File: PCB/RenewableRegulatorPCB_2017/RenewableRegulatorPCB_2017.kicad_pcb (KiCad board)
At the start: 2 copper layers, 77.5 x 81.9 mm, 59 parts, among them IC2 ATTINY85, K1 IO_0-2, K2 IO_3-5, K3 Vsense, K4 Vpower, P1 FTDI_OUTPUT, P11 Voutput, P12 Vsense, P13 OUT, P14 FET_IN, P2 IN, P3 Vinput, P4 5V, P5 ISP, P6 GND, P7 S_INPUT, P8 Vd, P9 Vg, Q1 PNP, Q2 NPN, Q3 MOSFET_N, SW1 SW_PUSH, U1 7805/LM2931, U2 LM7812, U3 AUIRS2124

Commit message: Updated PCB
First version of schematic. Needs review
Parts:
- removed BZ1: BUZZER, BUZZER_lg_pads
- removed IC2: ATTINY85, TRINKET
- removed K1: IO_0-2, SIL-3_lg_pad_1mm
- removed K2: IO_3-5, SIL-3_lg_pad_1mm
- removed K3: Vsense, SIL-3_lg_pad_1mm_marker
- removed K4: Vpower, SIL-3_lg_pad_1mm_marker
- removed MH1, MH2, MH3, MH4: CONN_1, 1pin_3mmhole
- removed P11: Voutput, 1pin_1.2mm
- removed P12: Vsense, 1pin_1.2mm
- removed P13: OUT, SIL_2_screw_blocks
- removed P14: FET_IN, 1pin_1.2mm
- removed P6: GND, 1pin_1.2mm
- removed P7: S_INPUT, SIL-6_large_pads_marker
- removed P8: Vd, 1pin_1.2mm
- removed P9: Vg, 1pin_1.2mm
- removed Q2: NPN, TO92-EBC_large_pad
- removed Q3: MOSFET_N, TO220_VERT_BUZ11_matt
- removed SW1: SW_PUSH, SW_PUSH_SMALL_ml_large_hole
- removed VAL: OSHW_logo_small_back, OSHW_logo_small_back
- removed VAL: reinnovation_logo_15mm, reinnovation_logo_15mm
- added C10: 10uf, REInnovationFootprint:C_1V7_TH, F.Cu at (114.9, 95.9)
- added C9: 1uf, REInnovationFootprint:C_1V7_TH, F.Cu at (108.6, 85.7)
- added DISP1: OLED_I2C, matts_components:SIL-4_large_pad, F.Cu at (153.7, 130.8)
- added DISP2: SPI_LCD, matts_components:SIL-8_lg_pad_1mm, F.Cu at (195.6, 84.5)
- added ENC1: Encoder, REInnovationFootprint:TH_Encoder, F.Cu at (135.3, 153.7)
- added F1: 1A, REInnovationFootprint:TH_MC36188_FUSE, F.Cu at (145.4, 119.4)
- added J1: Arduino_Nano_Header, REInnovationFootprint:NANO_DIP_30_600, F.Cu at (227.3, 109.9)
- added L1: 22uH, REInnovationFootprint:TH_Inductor, F.Cu at (167.0, 136.5)
- added LOGO1: CONN_1, CuriousElectric3:CEC_Globe_10mm_FCU, F.Cu at (56.5, 163.8)
- added LOGO2: CONN_1, CuriousElectric3:CuriousElectric_flat_12mm, F.Cu at (55.2, 155.6)
- added R10: 8.2k, REInnovationFootprint:TH_Resistor_1, F.Cu at (174.0, 111.1)
- added VR2: VR, REInnovationFootprint:TH_MC36188_FUSE, F.Cu at (125.7, 98.4)
- C1: value 10uf -> 100nf; footprint C1V7_lg_pad -> matts_components:C1_wide_lg_pad
- C2: value 100u -> 100nf; footprint C1V7_lg_pad -> matts_components:C1_wide_lg_pad
- C3: value 100n -> 100uf; footprint C1_wide_lg_pad -> REInnovationFootprint:C_1V7_TH
- C4, C5: value 10u -> 100nf; footprint C1V7_lg_pad -> matts_components:C1_wide_lg_pad
- C6: value 10u -> 2.2uf; footprint C1V7_lg_pad -> REInnovationFootprint:C_1V7_TH
- C7: value 100n -> 1uf; footprint C1_wide_lg_pad -> REInnovationFootprint:C_1V7_TH
- C8: value CP1 -> 100nf; footprint C1V7_lg_pad -> matts_components:C1_wide_lg_pad
- D1, D2: value 1N4001 -> 3v3; footprint D4_lg_pad -> REInnovationFootprint:TH_Diode_1
- D3: value VT2045BP -> 1N5819; footprint TO220_DIODE -> REInnovationFootprint:TH_Diode_1
- D4: value 1N4001 -> 1N5819; footprint D4_lg_pad -> REInnovationFootprint:TH_Diode_1
- D5: value 1N4148 -> WS2811_5mm; footprint D3_lg_pad -> REInnovationFootprint:TH_WS2811_LED_8mm
- D6: value UF4001 -> 1N5822; footprint D4_lg_pad -> REInnovationFootprint:TH_Diode_1
- D7: value 5v1 -> LED; footprint D3_lg_pad -> REInnovationFootprint:TH_LED-5MM_larg_pad
- D8: value DIODE -> UF4001; footprint D3_lg_pad -> REInnovationFootprint:TH_Diode_1
- D9: value GRN_LED -> 1N5819; footprint LED-5MM_larg_pad -> REInnovationFootprint:TH_Diode_1
- P1: value FTDI_OUTPUT -> INPUT; footprint SIL-6_large_pads_marker -> matts_components:SIL-2_screw_terminal_32A
- P2: value IN -> Vref?; footprint SIL_2_screw_blocks -> matts_components:SIL-2_solder_connect
- P3: value Vinput -> MicroSD; footprint 1pin_1.2mm -> matts_components:SIL-6_large_pads_marker
- P4: value 5V -> SERIAL; footprint 1pin_1.2mm -> matts_components:SIL-4_Grove_SIL
- P5: value ISP -> OUTPUT; footprint DIL_3x2_large_pads_1mm -> matts_components:SIL-2_screw_terminal_32A
- Q1: value PNP -> TK32A12N1; footprint TO92-EBC_large_pad -> matts_components:TO220_VERT_BUZ11_matt
- R1, R4: value 1k -> R; footprint R3-LARGE_PADS_0_8_hole -> REInnovationFootprint:TH_Resistor_1
- R2: value 100k -> R; footprint R3-LARGE_PADS_0_8_hole -> REInnovationFootprint:TH_Resistor_1
- R3: value 10k -> R; footprint R3-LARGE_PADS_0_8_hole -> REInnovationFootprint:TH_Resistor_1
- R5: value 10k -> 5; footprint R3-LARGE_PADS_0_8_hole -> REInnovationFootprint:TH_Resistor_1
- R6: value 330 -> 1k; footprint R3-LARGE_PADS_0_8_hole -> REInnovationFootprint:TH_Resistor_1
- R7, R8: value R -> 100k; footprint R3-LARGE_PADS_0_8_hole -> REInnovationFootprint:TH_Resistor_1
- R9: value 10 -> 100k; footprint R3-LARGE_PADS_0_8_hole -> REInnovationFootprint:TH_Resistor_1
- U1: value 7805/LM2931 -> IR2117; footprint TO92_7805_matt -> REInnovationFootprint:DIP-8_300_ELL
- U2: value LM7812 -> LMR16006; footprint TO92_7805_matt -> matts_components:SOT23-5_matt
- U3: value AUIRS2124 -> MCP1702-50; footprint SO8E -> matts_components:TO92_MCP9701_matt
- VR1: value P6KE33CA-E3 -> VR; footprint D4_lg_pad -> REInnovationFootprint:TH_MC36188_FUSE
- moved U1 102.7 mm to (203.2, 134.0), turned to 0 degrees
- moved C2 87.9 mm to (181.6, 143.5), turned to 0 degrees
- moved C3 83.8 mm to (84.5, 101.6), turned to 0 degrees
- moved C6 82.5 mm to (103.5, 133.3), turned to 0 degrees
- moved D3 78.9 mm to (144.1, 144.1), turned to 0 degrees
- moved P3 75.1 mm to (198.1, 89.5), turned to 0 degrees
- moved C8 66.7 mm to (94.0, 88.3), turned to 0 degrees
- moved D5 64.2 mm to (101.0, 71.8)
- moved R7 64.0 mm to (174.0, 103.5), turned to 0 degrees
- moved R8 59.9 mm to (174.0, 106.0), turned to 0 degrees
- moved Q1 59.0 mm to (182.9, 134.6), turned to 0 degrees
- moved C5 58.5 mm to (94.6, 83.8), turned to 0 degrees
- moved P4 58.1 mm to (127.0, 134.6)
- moved R6 58.0 mm to (174.0, 101.0), turned to 0 degrees
- moved D4 56.8 mm to (125.7, 71.8), turned to 0 degrees
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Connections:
- C1 pad 1: N-0000019 -> VINm
- C2 pad 1: +5V -> VOUTm
- C3 pad 1: GND -> Voutput
- C3 pad 2: +5V -> GND
- C4 pad 1: N-0000028 -> /Power Supply/+10V
- C5 pad 1: N-0000035 -> Net-(C5-Pad1)
- C5 pad 2: GND -> Voutput
- C6 pad 1: N-0000020 -> /Power Supply/+PWR
- C6 pad 2: Voutput -> GND
- C7 pad 1: SCK -> /Power Supply/+10V
- C8 pad 1: N-0000010 -> Net-(C8-Pad1)
- C8 pad 2: Voutput -> Net-(C8-Pad2)
- D1 pad 1: N-000009 -> GND
- D1 pad 2: N-0000019 -> VINm
- D2 pad 1: N-0000034 -> GND
- D2 pad 2: +5V -> VOUTm
- D3 pad 1: N-0000028 -> Net-(D3-Pad1)
- D3 pad 2: Vinput -> Voutput
- D4 pad 1: N-000008 -> Net-(D3-Pad1)
- D4 pad 2: +5V -> Vinput
- D5 pad 1: N-0000035 -> (no net)
- D5 pad 2: N-0000020 -> GND
- D6 pad 1: GND -> Net-(C5-Pad1)
- D6 pad 2: Voutput -> /Power Supply/+10V
- D7 pad 1: GND -> Voutput
- D7 pad 2: SCK -> Net-(D7-Pad2)
- D8 pad 1: N-0000035 -> GND
- D8 pad 2: N-0000010 -> Voutput
- D9 pad 1: N-000001 -> Net-(C8-Pad2)
- P1 pad 1: GND -> Vinput
- P2 pad 1: Vinput -> Net-(J1-Pad18)
- P2 pad 2: GND -> +3V3
- P3 pad 1: Vinput -> +3V3
- P4 pad 1: +5V -> GND
- P5 pad 1: LED -> Voutput
- P5 pad 2: N-000008 -> GND
- R1 pad 1: FET -> Vinput
- R1 pad 2: N-000007 -> VINm
- R2 pad 1: N-0000031 -> VINm
- R3 pad 1: N-0000031 -> Voutput
- R3 pad 2: N-000003 -> VOUTm
- R4 pad 1: N-0000020 -> VOUTm
- R4 pad 2: N-0000021 -> GND
- R5 pad 1: FET -> Net-(Q1-PadG)
- R5 pad 2: GND -> Net-(R5-Pad2)
- R6 pad 1: LED -> Net-(D7-Pad2)
- R6 pad 2: N-000001 -> GND
- R7 pad 1: N-000002 -> Net-(Q1-PadG)
- R7 pad 2: SCK -> Voutput
- R8 pad 1: SCK -> /Power Supply/+PWR
- R8 pad 2: GND -> Net-(R8-Pad2)
- R9 pad 1: N-0000011 -> /Power Supply/+10V
- R9 pad 2: N-0000021 -> Net-(R10-Pad1)
- VR1 pad 1: GND -> Vinput
- VR1 pad 2: N-0000028 -> GND
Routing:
- net GND: track 270.7 -> 0.00 mm, vias 1 -> 0
- net Voutput: track 225.9 -> 0.00 mm, vias 2 -> 0
- net Vinput: track 174.6 -> 0.00 mm
- net +5V: track 136.9 -> 0.00 mm, vias 3 -> 0
- net Tx: track 125.5 -> 0.00 mm, vias 3 -> 0
- net Rx: track 121.1 -> 0.00 mm, vias 1 -> 0
- net SCK: track 98.5 -> 0.00 mm
- net LED: track 91.0 -> 0.00 mm, vias 2 -> 0
- net N-0000028: track 62.4 -> 0.00 mm
- net FET: track 62.3 -> 0.00 mm
- net N-0000021: track 52.0 -> 0.00 mm
- net RESET: track 46.8 -> 0.00 mm
- net N-0000035: track 42.8 -> 0.00 mm, vias 1 -> 0
- net N-0000031: track 22.4 -> 0.00 mm
- net N-0000010: track 19.4 -> 0.00 mm
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- removed copper zone on B.Cu, net GND
- removed copper zone on F.Cu, net GND
- removed copper zone on F.Cu, net N-0000028
- removed copper zone on B.Cu, net Vinput
- removed copper zone on B.Cu, net Voutput
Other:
- board outline removed
- board text removed: "5/12/13 V1.2"
- board text removed: "DIODE"
- board text removed: "FET"
- board text removed: "I/O"
- board text removed: "Open Charge Regulator"
- board text removed: "TRINKET"
- board text removed: "re-innovation.co.uk"
- board text removed: "samaenergy.org"
- board text removed: "uP"

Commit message: Large update of PCB design
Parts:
- added J2: Arduino_Nano_Header, REInnovationFootprint:NANO_DIP_30_600, F.Cu at (153.7, 102.9)
- added P10: TP_FET, matts_components:1pin_0_8mm, F.Cu at (88.3, 121.3)
- added P11: TP_GND, matts_components:1pin_0_8mm, F.Cu at (78.7, 81.3)
- added P12: TP_5V, matts_components:1pin_0_8mm, F.Cu at (108.6, 59.1)
- added P13: TP_10V, matts_components:1pin_0_8mm, F.Cu at (104.1, 74.3)
- added P6: SERIAL, matts_components:SIL-4_Grove_SIL, F.Cu at (166.4, 87.6)
- added P7: A2, matts_components:SIL-4_Grove_SIL, F.Cu at (166.4, 78.1)
- added P8: TP_Vin, matts_components:1pin_0_8mm, F.Cu at (123.8, 84.5)
- added P9: TP_Vout, matts_components:1pin_0_8mm, F.Cu at (118.7, 108.6)
- added PCB1: PCB, REInnovationFootprint:PCB_75x100mm, F.Cu at (175.9, 130.2)
- added R11: 8.2k, REInnovationFootprint:TH_Resistor_1, F.Cu at (99.7, 81.3)
- DISP1: footprint matts_components:SIL-4_large_pad -> REInnovationFootprint:TH_OLED1306
- DISP2: footprint matts_components:SIL-8_lg_pad_1mm -> REInnovationFootprint:TH_LCD_SPI_128x128
- J1: value Arduino_Nano_Header -> JACK_TRS_6PINS; footprint REInnovationFootprint:NANO_DIP_30_600 -> REInnovationFootprint:TH_3_5mm_Jack
- LOGO1: value CONN_1 -> LOGO
- LOGO2: value CONN_1 -> LOGO; footprint CuriousElectric3:CuriousElectric_flat_12mm -> CuriousElectric3:TCEC_Words_13mm
- P4: value SERIAL -> A6_7
- R1, R3: value R -> Rb
- R10: value 8.2k -> 100k
- R2, R4: value R -> Ra
- R5: value 5 -> 4k7
- R6: value 1k -> 5
- R7: value 100k -> 1k
- U2: footprint matts_components:SOT23-5_matt -> REInnovationFootprint:SM_SOT23-6
- moved LOGO1 129.4 mm to (151.1, 75.6)
- moved U1 121.2 mm to (86.4, 101.6), turned to 180 degrees
- moved LOGO2 116.8 mm to (145.4, 81.3)
- moved U3 112.9 mm to (95.9, 59.7), turned to 180 degrees
- moved Q1 107.8 mm to (78.7, 106.7), turned to 180 degrees
- moved L1 95.2 mm to (98.4, 70.5)
- moved P1 92.3 mm to (88.9, 137.2)
- moved R7 90.4 mm to (85.7, 123.2), turned to 270 degrees
- moved R9 90.0 mm to (88.3, 81.3), turned to 270 degrees
- moved R8 86.1 mm to (88.3, 113.7), turned to 90 degrees
- moved R6 83.5 mm to (91.4, 113.7), turned to 90 degrees
- moved R10 83.0 mm to (96.5, 81.3), turned to 270 degrees
- moved U2 82.7 mm to (82.5, 78.1), turned to 270 degrees
- moved P4 76.9 mm to (166.4, 68.6)
- moved C2 74.5 mm to (118.7, 103.5), turned to 90 degrees
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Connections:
- J1 pad 1: Tx -> GND
- J1 pad 2: Rx -> +5V
- J1 pad 3: (no net) -> TEMP
- J1 pad 5: EN_A -> (no net)
- J1 pad 6: EN_B -> (no net)
- P2 pad 1: Net-(J1-Pad18) -> Net-(J2-Pad18)
- P4 pad 3: Tx -> A7
- P4 pad 4: Rx -> A6
- Q1 pad G: Net-(Q1-PadG) -> Net-(P10-Pad1)
- R10 pad 1: Net-(R10-Pad1) -> /Power Supply/+10V
- R10 pad 2: GND -> Net-(R10-Pad2)
- R5 pad 1: Net-(Q1-PadG) -> +5V
- R5 pad 2: Net-(R5-Pad2) -> TEMP
- R6 pad 1: Net-(D7-Pad2) -> Net-(P10-Pad1)
- R6 pad 2: GND -> Net-(R6-Pad2)
- R7 pad 1: Net-(Q1-PadG) -> Net-(D7-Pad2)
- R7 pad 2: Voutput -> GND
- R8 pad 1: /Power Supply/+PWR -> Net-(P10-Pad1)
- R8 pad 2: Net-(R8-Pad2) -> Voutput
- R9 pad 1: /Power Supply/+10V -> /Power Supply/+PWR
- R9 pad 2: Net-(R10-Pad1) -> Net-(R9-Pad2)
- U1 pad 7: Net-(R5-Pad2) -> Net-(R6-Pad2)
- U2 pad 3: Net-(R10-Pad1) -> Net-(R10-Pad2)
- U2 pad 4: Net-(R8-Pad2) -> Net-(R9-Pad2)

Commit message: First Version of PCB
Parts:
- removed PCB1: PCB, REInnovationFootprint:PCB_75x100mm
- moved P7 102.0 mm to (70.5, 43.2), turned to 180 degrees
- moved P6 93.8 mm to (83.8, 43.2), turned to 180 degrees
- moved P3 80.1 mm to (147.3, 47.6), turned to 180 degrees
- moved P2 74.1 mm to (109.9, 46.4), turned to 90 degrees
- moved P4 73.7 mm to (97.2, 43.2), turned to 180 degrees
- moved R7 64.3 mm to (104.1, 61.6), turned to 90 degrees
- moved D8 59.2 mm to (108.0, 62.9), turned to 90 degrees
- moved J2 59.0 mm to (120.7, 54.0), turned to 90 degrees
- moved R6 55.9 mm to (89.5, 57.8), turned to 180 degrees
- moved D6 55.7 mm to (74.9, 50.8), turned to 0 degrees
- moved C5 55.3 mm to (96.5, 56.5)
- moved R8 53.4 mm to (100.3, 61.6), turned to 270 degrees
- moved D7 53.1 mm to (104.1, 70.5), turned to 270 degrees
- moved C4 44.7 mm to (67.3, 56.5), turned to 270 degrees
- moved LOGO2 43.6 mm to (157.5, 39.4)
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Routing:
- net GND: track 0.00 -> 575.2 mm
- net +5V: track 0.00 -> 244.0 mm, vias 0 -> 1
- net Voutput: track 0.00 -> 146.5 mm
- net TEMP: track 0.00 -> 145.8 mm, vias 0 -> 1
- net FET1: track 0.00 -> 107.0 mm
- net VOUTm: track 0.00 -> 105.0 mm
- net SCK: track 0.00 -> 100.5 mm, vias 0 -> 1
- net Rx: track 0.00 -> 94.9 mm, vias 0 -> 1
- net /Power Supply/+10V: track 0.00 -> 93.3 mm
- net Tx: track 0.00 -> 91.3 mm, vias 0 -> 1
- net Vinput: track 0.00 -> 86.8 mm
- net VINm: track 0.00 -> 86.6 mm
- net Net-(P10-Pad1): track 0.00 -> 80.7 mm
- net A7: track 0.00 -> 76.3 mm
- net A6: track 0.00 -> 74.3 mm
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- added copper zone on F.Cu, net Vinput
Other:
- net class Default: trace_width 2.54 -> 0.5

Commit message: Secod
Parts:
- C10: footprint REInnovationFootprint:C_1V7_TH -> RenewableRegulatorPCB_2017_Library_Yoan:Capacitor_C10_1V7_TH
- C3: footprint REInnovationFootprint:C_1V7_TH -> RenewableRegulatorPCB_2017_Library_Yoan:Capacitor_C_1V7_TH
- C6: footprint REInnovationFootprint:C_1V7_TH -> RenewableRegulatorPCB_2017_Library_Yoan:Capacitor_C6_1V7_TH
- C7: footprint REInnovationFootprint:C_1V7_TH -> RenewableRegulatorPCB_2017_Library_Yoan:Capacitor_C7_1V7_TH
- C9: footprint REInnovationFootprint:C_1V7_TH -> RenewableRegulatorPCB_2017_Library_Yoan:Capacitor_C9_1V7_TH
- P1, P5: footprint matts_components:SIL-2_screw_terminal_32A -> RenewableRegulatorPCB_2017_Library_Yoan:Connecteurs_IO_SIL-2_screw_terminal_32A
- moved LOGO2 103.8 mm to (71.6, 97.8)
- moved LOGO1 62.9 mm to (116.8, 75.4)
- moved D8 33.0 mm to (101.6, 95.2), turned to 180 degrees
- moved R7 30.1 mm to (100.3, 91.4), turned to 180 degrees
- moved R6 29.2 mm to (88.9, 87.0), turned to 90 degrees
- moved C9 26.9 mm to (103.8, 63.6), turned to 90 degrees
- moved R8 26.7 mm to (100.3, 88.3), turned to 0 degrees
- moved C5 26.4 mm to (92.1, 82.5)
- moved U1 26.3 mm to (75.6, 88.9)
- moved C4 26.0 mm to (66.7, 82.5)
- moved D6 26.0 mm to (74.9, 76.8)
- moved D7 23.9 mm to (111.1, 93.3)
- moved P1 17.6 mm to (90.2, 134.0)
- moved P5 17.6 mm to (111.8, 134.0)
- moved U3 15.2 mm to (103.8, 71.4), turned to 0 degrees
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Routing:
- net GND: track 575.2 -> 379.8 mm
- net TEMP: track 145.8 -> 80.6 mm, vias 1 -> 0
- net LED_D: track 33.8 -> 97.1 mm
- net SCK: track 100.5 -> 53.2 mm
- net VOUTm: track 105.0 -> 58.4 mm
- net +5V: track 244.0 -> 204.5 mm
- net A6: track 74.3 -> 35.8 mm, vias 0 -> 3
- net A7: track 76.3 -> 38.5 mm, vias 0 -> 4
- net Net-(P10-Pad1): track 80.7 -> 44.5 mm
- net SCL: track 61.6 -> 95.8 mm, vias 1 -> 2
- net Voutput: track 146.5 -> 123.8 mm
- net VINm: track 86.6 -> 68.2 mm
- net Rx: track 94.9 -> 80.5 mm, vias 1 -> 0
- net SD_CS: track 35.7 -> 21.8 mm, vias 0 -> 1
- net Vinput: track 86.8 -> 100.0 mm
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- added copper zone on B.Cu, net GND
- added copper zone on F.Cu, net GND
- added copper zone on F.Cu, net Voutput
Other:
- board outline added: 99.7 x 88.3 mm
- net class Thick: trace_width 5.08 -> 5

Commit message: Third Version of PCB
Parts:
- added MH1: CONN_1, RenewableRegulatorPCB_2017_Library_Yoan:3mm_hole, F.Cu at (161.0, 114.1)
- added MH1: CONN_1, RenewableRegulatorPCB_2017_Library_Yoan:3mm_hole, F.Cu at (161.0, 49.1)
- added MH1: CONN_1, RenewableRegulatorPCB_2017_Library_Yoan:3mm_hole, F.Cu at (66.0, 49.1)
- added MH1: CONN_1, RenewableRegulatorPCB_2017_Library_Yoan:3mm_hole, F.Cu at (66.0, 114.1)
- moved P7 4.79 mm to (72.9, 56.5)
- moved P6 2.10 mm to (85.3, 54.0)
- moved LOGO2 1.44 mm to (70.6, 96.8)
- moved P12 0.74 mm to (116.5, 92.1)
- moved DISP1 0.63 mm to (144.8, 64.8)
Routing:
- net GND: track 379.8 -> 363.9 mm
- net FET1: track 118.6 -> 114.7 mm
- net A2: track 49.9 -> 46.4 mm
- net +5V: track 204.5 -> 207.8 mm
- net Voutput: track 123.8 -> 126.3 mm
- net Rx: track 80.5 -> 81.3 mm
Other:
- board size 99.7 x 88.3 mm -> 101.3 x 88.3 mm

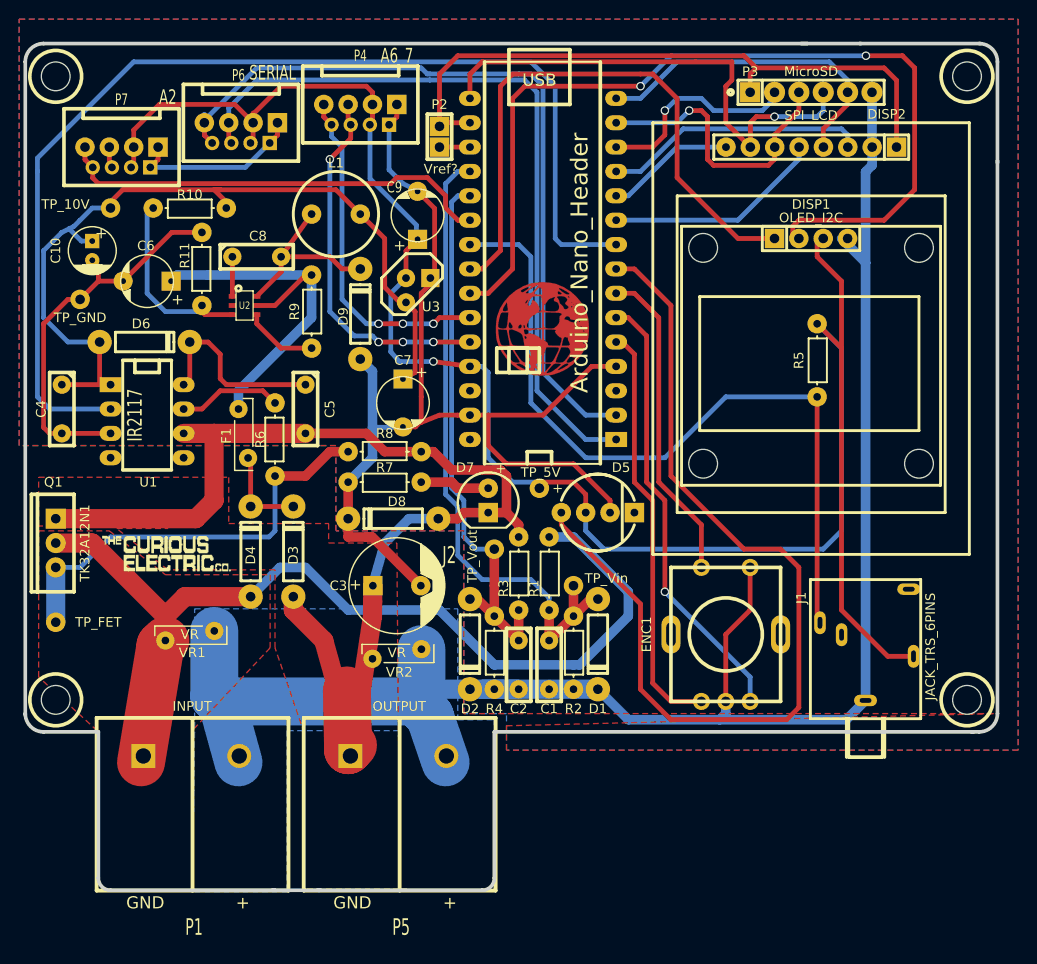
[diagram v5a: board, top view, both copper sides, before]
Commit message: Updated PCB and schematic
WS2811 LED swapped around Vcc and GND
OLED swapped around for front mounting
Tracks cleaned up
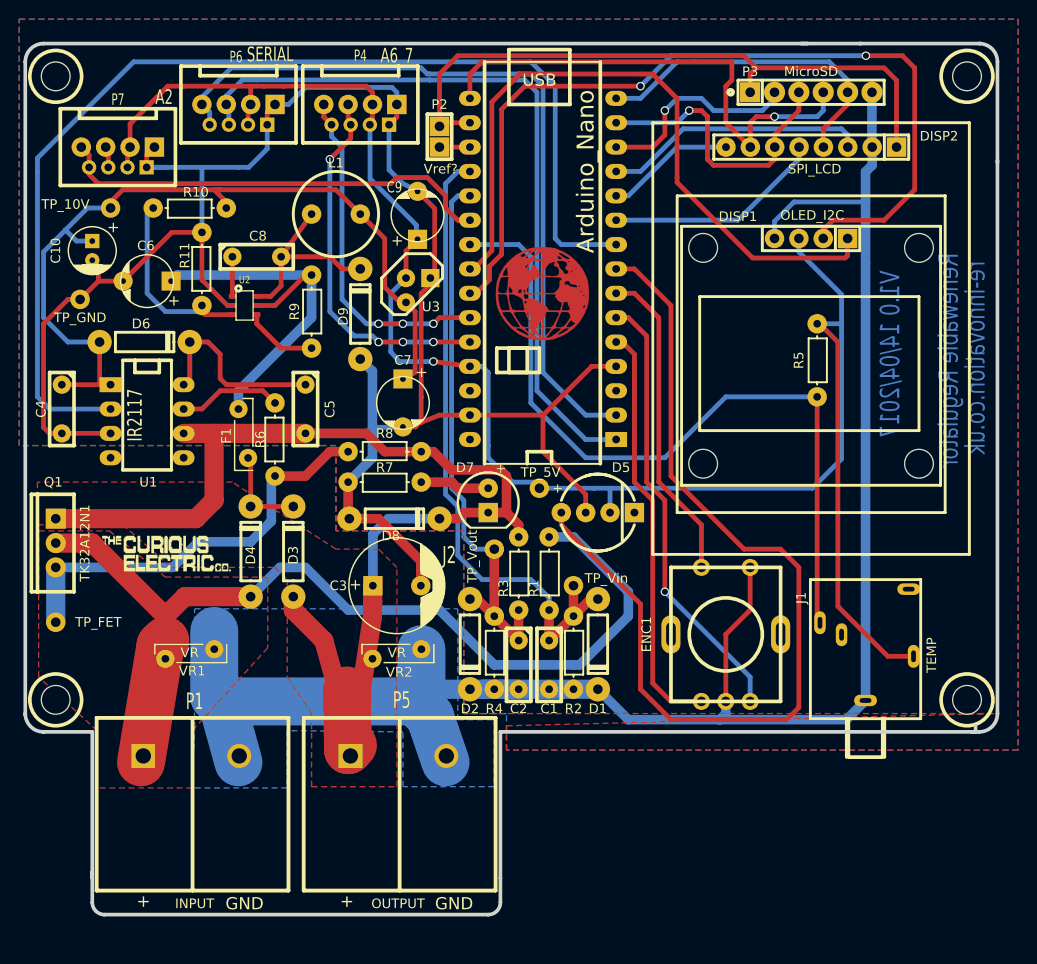
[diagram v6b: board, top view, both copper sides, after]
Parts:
- D5: value WS2811_5mm -> WS2811_EpiStar_8mm
- D8: value UF4001 -> UF4002
- DISP1: footprint REInnovationFootprint:TH_OLED1306 -> TH_OLED1306
- F1: value 1A -> 500mA
- J1: value JACK_TRS_6PINS -> TEMP
- J2: value Arduino_Nano_Header -> Arduino_Nano
- MH1: value CONN_1 -> Mounting holes
- moved LOGO1 3.68 mm to (116.8, 71.8)
- moved P6 1.92 mm to (85.1, 52.1)
- moved VR1 1.91 mm to (77.5, 109.9)
- moved D8 0.63 mm to (101.0, 95.2), turned to 0 degrees
- moved P7 0.38 mm to (72.5, 56.5)
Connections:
- D5 pad 2: GND -> +5V
- D5 pad 3: +5V -> GND
- D8 pad 1: GND -> Voutput
- D8 pad 2: Voutput -> GND
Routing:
- net GND: track 363.9 -> 400.3 mm
- net Voutput: track 126.3 -> 139.1 mm
- net Vinput: track 100.0 -> 111.1 mm
- net SDA: track 61.5 -> 71.8 mm
- net +5V: track 207.8 -> 198.4 mm
- net SCL: track 95.8 -> 91.7 mm
- net Rx: track 81.3 -> 80.1 mm
- net Tx: track 79.1 -> 78.2 mm
- net Net-(C8-Pad2): track 19.4 -> 20.3 mm
- net Net-(P10-Pad1): track 44.5 -> 43.7 mm
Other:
- board size 101.3 x 88.3 mm -> 101.3 x 90.8 mm
- board text added: "Renewable Regulator"
- board text added: "V1.0 14/04/2017"
- board text added: "re-innovation.co.uk"

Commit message: Minor PCb changes. Fit to 100mm x 100mm
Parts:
- moved MH1 2.54 mm to (158.5, 114.2)
- moved MH1 2.54 mm to (158.5, 49.1)
- moved J1 1.02 mm to (155.2, 101.6)
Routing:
- net GND: track 400.3 -> 402.6 mm
- net +5V: track 198.4 -> 197.8 mm
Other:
- board size 101.3 x 90.8 mm -> 99.6 x 90.8 mm
- net class Default: trace_width 0.5 -> 1
- board text added: "curiouselectric.co.uk"
- board text removed: "re-innovation.co.uk"

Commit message: Regulator PCB changes
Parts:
- L1: footprint REInnovationFootprint:TH_Inductor -> REInnovationFootprint:TH_Inductor2
- U3: footprint matts_components:TO92_MCP9701_matt -> REInnovationFootprint:TO92_MCP9701_matt2
- moved D5 49.4 mm to (87.0, 60.3)
- moved P12 7.19 mm to (123.2, 94.6)
- moved D7 5.49 mm to (116.6, 92.7)
- moved U3 3.01 mm to (101.0, 72.4)
- moved MH1 2.54 mm to (161.0, 114.1)
- moved MH1 2.54 mm to (161.0, 49.1)
- moved R10 1.27 mm to (80.0, 64.1)
- moved R11 1.27 mm to (81.3, 70.5)
- moved VR1 1.27 mm to (76.2, 109.9)
- moved J1 1.02 mm to (156.2, 101.6)
- moved L1 0.90 mm to (95.9, 64.1)
- moved VR2 0.64 mm to (98.4, 109.9)
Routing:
- net GND: track 402.6 -> 366.7 mm
- net Voutput: track 139.1 -> 128.2 mm
- net Net-(D7-Pad2): track 7.25 -> 12.5 mm
- net +5V: track 197.8 -> 202.3 mm
- net /Power Supply/+10V: track 89.0 -> 93.2 mm
- net LED_D: track 97.1 -> 94.3 mm, vias 0 -> 3
- net Net-(R10-Pad2): track 20.1 -> 17.8 mm
- net Net-(C8-Pad2): track 20.3 -> 18.1 mm
- net A2: track 46.1 -> 47.9 mm
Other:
- board size 99.6 x 90.8 mm -> 101.3 x 90.8 mm
- net class Default: trace_width 1 -> 2
- board text added: "re-innovation.co.uk"
- board text removed: "curiouselectric.co.uk"
